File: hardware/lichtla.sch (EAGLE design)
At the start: 45 parts, among them J1 Power supply, J10 LED5, J11 LED6, J12 LED7, J13 PWM Interface, J14 BLE Nano Interface, J2 HEADER0, J3 HEADER1, J4 USB, J5 LED0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

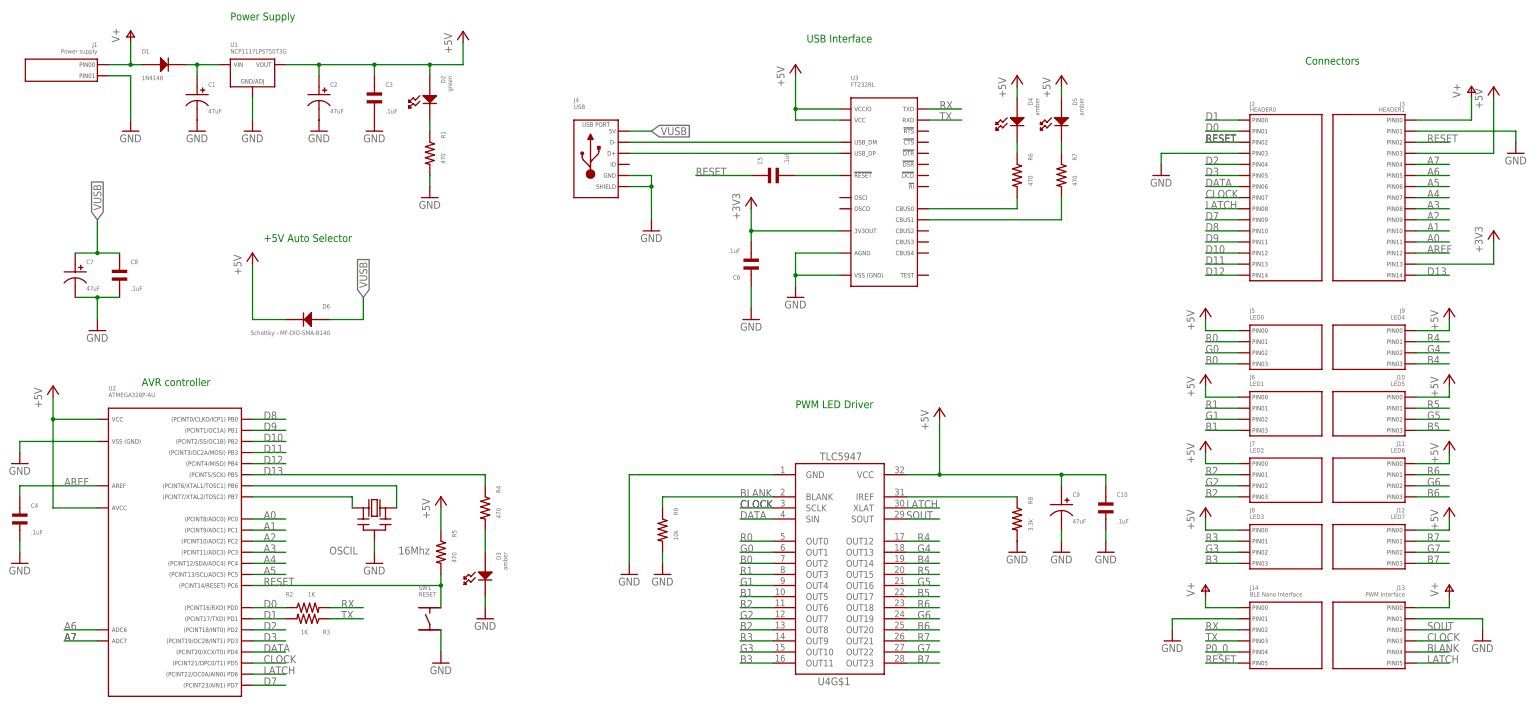
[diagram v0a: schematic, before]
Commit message: Added interface for Bluefruit LE UART Friend
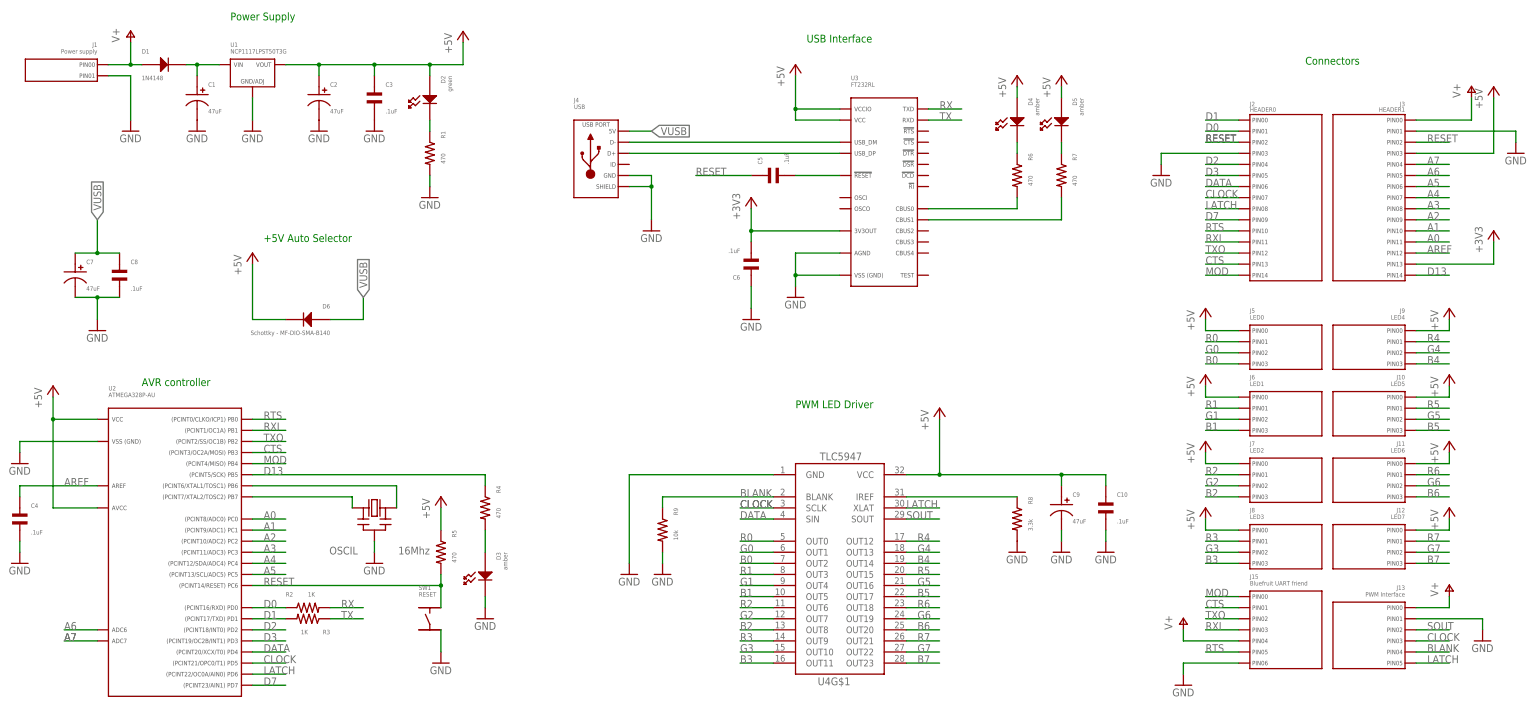
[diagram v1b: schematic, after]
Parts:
- removed J14: BLE Nano Interface, MF_Connectors:HEADER_01X06_PTH_2.54MM
- added J15: Bluefruit UART friend, MF_Connectors:HEADER_01X07_PTH_2.54MM
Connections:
- removed net D10: J2.PIN12, U2.PB2
- removed net D11: J2.PIN13, U2.PB3
- removed net D12: J2.PIN14, U2.PB4
- removed net D8: J2.PIN10, U2.PB0
- removed net D9: J2.PIN11, U2.PB1
- removed net P0_0: J14.PIN4
- new net CTS: J15.PIN1, J2.PIN13, U2.PB3
- new net MOD: J15.PIN0, J2.PIN14, U2.PB4
- new net RTS: J15.PIN5, J2.PIN10, U2.PB0
- new net RXI: J15.PIN3, J2.PIN11, U2.PB1
- new net TXO: J15.PIN2, J2.PIN12, U2.PB2
- net GND: now also J15.PIN6; no longer J14.PIN1
- net RESET: no longer J14.PIN5
- net RX: no longer J14.PIN2
- net TX: no longer J14.PIN3
- net V+: now also J15.PIN4; no longer J14.PIN0
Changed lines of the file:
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@@
 <part name="GND23" library="supply1" deviceset="GND" device=""/>
 <part name="P+23" library="supply1" deviceset="V+" device=""/>
-<part name="J14" library="MF_Connectors" deviceset="HEADER_01X06" device="_PTH_2.54MM" value="BLE Nano Interface"/>
-<part name="P+4" library="supply1" deviceset="V+" device=""/>
-<part name="GND24" library="supply1" deviceset="GND" device=""/>
+<part name="J15" library="MF_Connectors" deviceset="HEADER_01X07" device="_PTH_2.54MM" value="Bluefruit UART friend"/>
+<part name="P+5" library="supply1" deviceset="V+" device=""/>
+<part name="GND25" library="supply1" deviceset="GND" device=""/>
 </parts>
 <sheets>
@@
 <instance part="GND23" gate="1" x="228.6" y="-12.7"/>
 <instance part="P+23" gate="1" x="-81.28" y="127"/>
-<instance part="J14" gate="G$1" x="175.26" y="-5.08"/>
-<instance part="P+4" gate="1" x="165.1" y="0"/>
-<instance part="GND24" gate="1" x="157.48" y="-12.7"/>
+<instance part="J15" gate="G$1" x="175.26" y="-2.54"/>
+<instance part="P+5" gate="1" x="160.02" y="-7.62"/>
+<instance part="GND25" gate="1" x="160.02" y="-22.86"/>
 </instances>
 <busses>
@@
 </segment>
 <segment>
-<pinref part="J14" gate="G$1" pin="PIN1"/>
-<wire x1="172.72" y1="-7.62" x2="157.48" y2="-7.62" width="0.1524" layer="91"/>
-<pinref part="GND24" gate="1" pin="GND"/>
-<wire x1="157.48" y1="-7.62" x2="157.48" y2="-10.16" width="0.1524" layer="91"/>
+<pinref part="J15" gate="G$1" pin="PIN6"/>
+<wire x1="172.72" y1="-17.78" x2="160.02" y2="-17.78" width="0.1524" layer="91"/>
+<pinref part="GND25" gate="1" pin="GND"/>
+<wire x1="160.02" y1="-17.78" x2="160.02" y2="-20.32" width="0.1524" layer="91"/>
 </segment>
 </net>
@@
 <label x="48.26" y="93.98" size="1.778" layer="95"/>
 </segment>
-<segment>
-<pinref part="J14" gate="G$1" pin="PIN5"/>
-<wire x1="172.72" y1="-17.78" x2="165.1" y2="-17.78" width="0.1524" layer="91"/>
-<label x="165.1" y="-17.78" size="1.778" layer="95"/>
-</segment>
 </net>
 <net name="D13" class="0">
@@
 <wire x1="172.72" y1="83.82" x2="165.1" y2="83.82" width="0.1524" layer="91"/>
 <label x="165.1" y="83.82" size="1.778" layer="95"/>
-</segment>
-</net>
-<net name="D8" class="0">
-<segment>
-<pinref part="U2" gate="G$1" pin="PB0"/>
-<wire x1="-53.34" y1="38.1" x2="-45.72" y2="38.1" width="0.1524" layer="91"/>
-<label x="-50.8" y="38.1" size="1.778" layer="95"/>
-</segment>
-<segment>
-<pinref part="J2" gate="G$1" pin="PIN10"/>
-<wire x1="172.72" y1="81.28" x2="165.1" y2="81.28" width="0.1524" layer="91"/>
-<label x="165.1" y="81.28" size="1.778" layer="95"/>
-</segment>
-</net>
-<net name="D9" class="0">
-<segment>
-<pinref part="U2" gate="G$1" pin="PB1"/>
-<wire x1="-53.34" y1="35.56" x2="-45.72" y2="35.56" width="0.1524" layer="91"/>
-<label x="-50.8" y="35.56" size="1.778" layer="95"/>
-</segment>
-<segment>
-<pinref part="J2" gate="G$1" pin="PIN11"/>
-<wire x1="172.72" y1="78.74" x2="165.1" y2="78.74" width="0.1524" layer="91"/>
-<label x="165.1" y="78.74" size="1.778" layer="95"/>
-</segment>
-</net>
-<net name="D10" class="0">
-<segment>
-<pinref part="U2" gate="G$1" pin="PB2"/>
-<wire x1="-53.34" y1="33.02" x2="-45.72" y2="33.02" width="0.1524" layer="91"/>
-<label x="-50.8" y="33.02" size="1.778" layer="95"/>
-</segment>
-<segment>
-<pinref part="J2" gate="G$1" pin="PIN12"/>
-<wire x1="172.72" y1="76.2" x2="165.1" y2="76.2" width="0.1524" layer="91"/>
-<label x="165.1" y="76.2" size="1.778" layer="95"/>
-</segment>
-</net>
-<net name="D11" class="0">
-<segment>
-<pinref part="U2" gate="G$1" pin="PB3"/>
-<wire x1="-53.34" y1="30.48" x2="-45.72" y2="30.48" width="0.1524" layer="91"/>
-<label x="-50.8" y="30.48" size="1.778" layer="95"/>
-</segment>
-<segment>
-<pinref part="J2" gate="G$1" pin="PIN13"/>
-<wire x1="172.72" y1="73.66" x2="165.1" y2="73.66" width="0.1524" layer="91"/>
-<label x="165.1" y="73.66" size="1.778" layer="95"/>
-</segment>
-</net>
-<net name="D12" class="0">
-<segment>
-<pinref part="U2" gate="G$1" pin="PB4"/>
-<wire x1="-53.34" y1="27.94" x2="-45.72" y2="27.94" width="0.1524" layer="91"/>
-<label x="-50.8" y="27.94" size="1.778" layer="95"/>
-</segment>
-<segment>
-<pinref part="J2" gate="G$1" pin="PIN14"/>
-<wire x1="172.72" y1="71.12" x2="165.1" y2="71.12" width="0.1524" layer="91"/>
-<label x="165.1" y="71.12" size="1.778" layer="95"/>
 </segment>
 </net>
@@
 </segment>
 <segment>
-<pinref part="J14" gate="G$1" pin="PIN0"/>
-<wire x1="172.72" y1="-5.08" x2="165.1" y2="-5.08" width="0.1524" layer="91"/>
-<pinref part="P+4" gate="1" pin="V+"/>
-<wire x1="165.1" y1="-5.08" x2="165.1" y2="-2.54" width="0.1524" layer="91"/>
+<pinref part="J15" gate="G$1" pin="PIN4"/>
+<wire x1="172.72" y1="-12.7" x2="160.02" y2="-12.7" width="0.1524" layer="91"/>
+<pinref part="P+5" gate="1" pin="V+"/>
+<wire x1="160.02" y1="-12.7" x2="160.02" y2="-10.16" width="0.1524" layer="91"/>
 </segment>
 </net>
@@
 <label x="104.14" y="109.22" size="1.778" layer="95"/>
 </segment>
-<segment>
-<pinref part="J14" gate="G$1" pin="PIN2"/>
-<wire x1="172.72" y1="-10.16" x2="165.1" y2="-10.16" width="0.1524" layer="91"/>
-<label x="165.1" y="-10.16" size="1.778" layer="95"/>
-</segment>
 </net>
 <net name="TX" class="0">
@@
 <wire x1="101.6" y1="106.68" x2="109.22" y2="106.68" width="0.1524" layer="91"/>
 <label x="104.14" y="106.68" size="1.778" layer="95"/>
-</segment>
-<segment>
-<pinref part="J14" gate="G$1" pin="PIN3"/>
-<wire x1="172.72" y1="-12.7" x2="165.1" y2="-12.7" width="0.1524" layer="91"/>
-<label x="165.1" y="-12.7" size="1.778" layer="95"/>
 </segment>
 </net>
@@
 </segment>
 </net>
-<net name="P0_0" class="0">
-<segment>
-<pinref part="J14" gate="G$1" pin="PIN4"/>
+<net name="MOD" class="0">
+<segment>
+<pinref part="J15" gate="G$1" pin="PIN0"/>
+<wire x1="172.72" y1="-2.54" x2="165.1" y2="-2.54" width="0.1524" layer="91"/>
+<label x="165.1" y="-2.54" size="1.778" layer="95"/>
+</segment>
+<segment>
+<pinref part="U2" gate="G$1" pin="PB4"/>
+<wire x1="-53.34" y1="27.94" x2="-45.72" y2="27.94" width="0.1524" layer="91"/>
+<label x="-50.8" y="27.94" size="1.778" layer="95"/>
+</segment>
+<segment>
+<pinref part="J2" gate="G$1" pin="PIN14"/>
+<wire x1="172.72" y1="71.12" x2="165.1" y2="71.12" width="0.1524" layer="91"/>
+<label x="165.1" y="71.12" size="1.778" layer="95"/>
+</segment>
+</net>
+<net name="CTS" class="0">
+<segment>
+<pinref part="J15" gate="G$1" pin="PIN1"/>
+<wire x1="172.72" y1="-5.08" x2="165.1" y2="-5.08" width="0.1524" layer="91"/>
+<label x="165.1" y="-5.08" size="1.778" layer="95"/>
+</segment>
+<segment>
+<pinref part="U2" gate="G$1" pin="PB3"/>
+<wire x1="-53.34" y1="30.48" x2="-45.72" y2="30.48" width="0.1524" layer="91"/>
+<label x="-50.8" y="30.48" size="1.778" layer="95"/>
+</segment>
+<segment>
+<pinref part="J2" gate="G$1" pin="PIN13"/>
+<wire x1="172.72" y1="73.66" x2="165.1" y2="73.66" width="0.1524" layer="91"/>
+<label x="165.1" y="73.66" size="1.778" layer="95"/>
+</segment>
+</net>
+<net name="TXO" class="0">
+<segment>
+<pinref part="J15" gate="G$1" pin="PIN2"/>
+<wire x1="172.72" y1="-7.62" x2="165.1" y2="-7.62" width="0.1524" layer="91"/>
+<label x="165.1" y="-7.62" size="1.778" layer="95"/>
+</segment>
+<segment>
+<pinref part="U2" gate="G$1" pin="PB2"/>
+<wire x1="-53.34" y1="33.02" x2="-45.72" y2="33.02" width="0.1524" layer="91"/>
+<label x="-50.8" y="33.02" size="1.778" layer="95"/>
+</segment>
+<segment>
+<pinref part="J2" gate="G$1" pin="PIN12"/>
+<wire x1="172.72" y1="76.2" x2="165.1" y2="76.2" width="0.1524" layer="91"/>
+<label x="165.1" y="76.2" size="1.778" layer="95"/>
+</segment>
+</net>
+<net name="RXI" class="0">
+<segment>
+<pinref part="J15" gate="G$1" pin="PIN3"/>
+<wire x1="172.72" y1="-10.16" x2="165.1" y2="-10.16" width="0.1524" layer="91"/>
+<label x="165.1" y="-10.16" size="1.778" layer="95"/>
+</segment>
+<segment>
+<pinref part="U2" gate="G$1" pin="PB1"/>
+<wire x1="-53.34" y1="35.56" x2="-45.72" y2="35.56" width="0.1524" layer="91"/>
+<label x="-50.8" y="35.56" size="1.778" layer="95"/>
+</segment>
+<segment>
+<pinref part="J2" gate="G$1" pin="PIN11"/>
+<wire x1="172.72" y1="78.74" x2="165.1" y2="78.74" width="0.1524" layer="91"/>
+<label x="165.1" y="78.74" size="1.778" layer="95"/>
+</segment>
+</net>
+<net name="RTS" class="0">
+<segment>
+<pinref part="J15" gate="G$1" pin="PIN5"/>
 <wire x1="172.72" y1="-15.24" x2="165.1" y2="-15.24" width="0.1524" layer="91"/>
 <label x="165.1" y="-15.24" size="1.778" layer="95"/>
 </segment>
-</net>
+<segment>
+<pinref part="U2" gate="G$1" pin="PB0"/>
+<wire x1="-53.34" y1="38.1" x2="-45.72" y2="38.1" width="0.1524" layer="91"/>
+<label x="-50.8" y="38.1" size="1.778" layer="95"/>
+</segment>
+<segment>
+<pinref part="J2" gate="G$1" pin="PIN10"/>
+<wire x1="172.72" y1="81.28" x2="165.1" y2="81.28" width="0.1524" layer="91"/>
+<label x="165.1" y="81.28" size="1.778" layer="95"/>
+</segment>
+</net>

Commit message: Updated schematic with less connectors
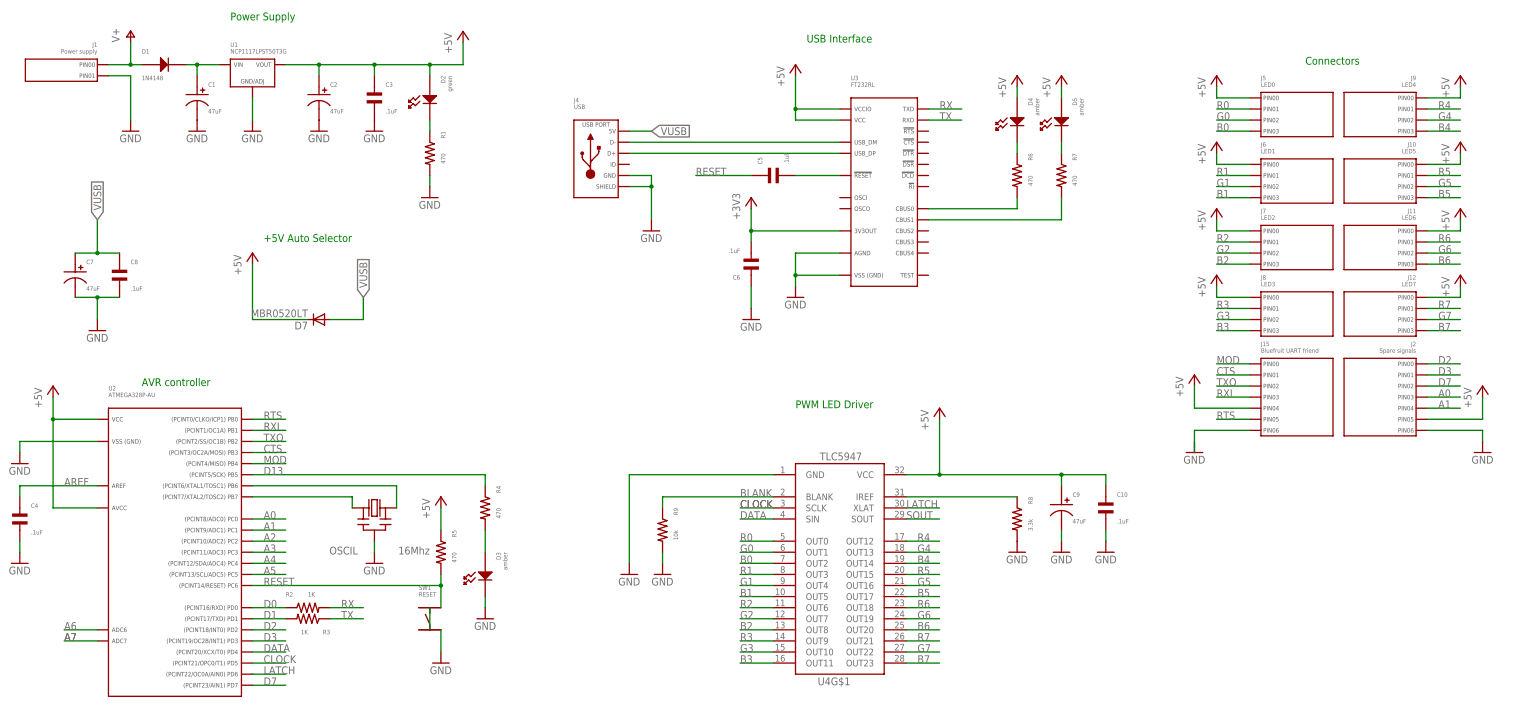
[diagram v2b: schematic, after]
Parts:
- removed D6: Schottky - MF-DIO-SMA-B140, MF_Discrete_Semiconductor:DIODE_SMA
- removed J13: PWM Interface, MF_Connectors:HEADER_01X06_PTH_2.54MM
- removed J3: HEADER1, MF_Connectors:HEADER_01X15_PTH_2.54MM
- added D7: MBR0520LT, diode:MBR0520LT
- J2: value HEADER0 -> Spare signals; device MF_Connectors:HEADER_01X15_PTH_2.54MM -> MF_Connectors:HEADER_01X07_PTH_2.54MM
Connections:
- net +3V3: no longer J3.PIN13
- net +5V: now also D7.C, J15.PIN4, J2.PIN5; no longer D6.CATHODE, J3.PIN3
- net A0: now also J2.PIN3; no longer J3.PIN11
- net A1: now also J2.PIN4; no longer J3.PIN10
- net A2: no longer J3.PIN9
- net A3: no longer J3.PIN8
- net A4: no longer J3.PIN7
- net A5: no longer J3.PIN6
- net A6: no longer J3.PIN5
- net A7: no longer J3.PIN4
- net AREF: no longer J3.PIN12
- net BLANK: no longer J13.PIN4
- net CLOCK: no longer J13.PIN3, J2.PIN7
- net CTS: no longer J2.PIN13
- net D0: no longer J2.PIN1
- net D1: no longer J2.PIN0
- net D13: no longer J3.PIN14
- net D2: now also J2.PIN0; no longer J2.PIN4
- net D3: now also J2.PIN1; no longer J2.PIN5
- net D7: now also J2.PIN2; no longer J2.PIN9
- net DATA: no longer J2.PIN6
- net GND: now also J2.PIN6; no longer J13.PIN1, J2.PIN3, J3.PIN1
- net LATCH: no longer J13.PIN5, J2.PIN8
- net MOD: no longer J2.PIN14
- net RESET: no longer J2.PIN2, J3.PIN2
- net RTS: no longer J2.PIN10
- net RXI: no longer J2.PIN11
- net SOUT: no longer J13.PIN2
- net TXO: no longer J2.PIN12
- net V+: no longer J13.PIN0, J15.PIN4, J3.PIN0
- net VUSB: now also D7.A; no longer D6.ANODE
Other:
- moved on the sheet: J10, J11, J12, J15, J5, J6, J7, J8, J9
